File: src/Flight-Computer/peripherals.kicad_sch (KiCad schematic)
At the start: 34 parts, among them P10 Micro_SD_Card, P8 USB, P9 1984659, Q5 QS5U17TR, Q6 QS5U17TR, U10 TS391IYLT, U11 TS391IYLT, U6 SST25VF040B-50-4I-S2AE-T, U7 RFM95W-868S2, U8 CP2102-GMR(QFN28), U9 TS391IYLT

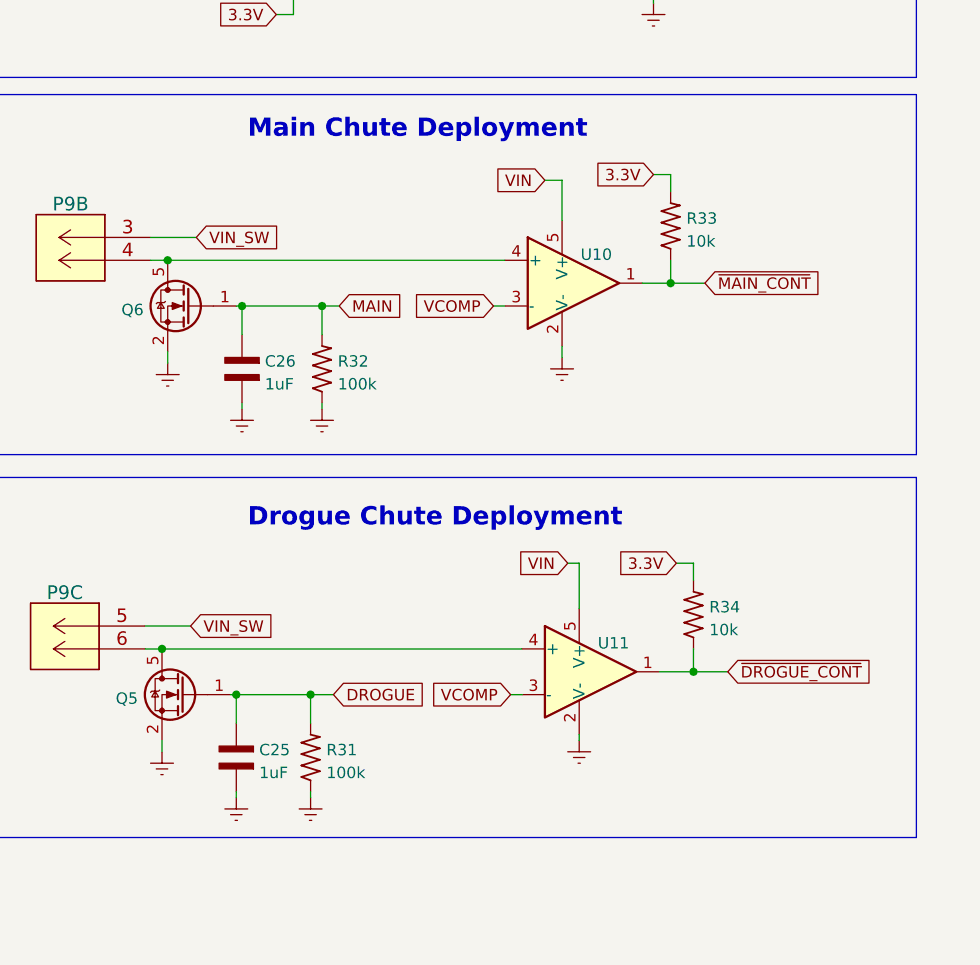
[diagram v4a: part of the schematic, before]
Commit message: added ignition continuity pull down resistors
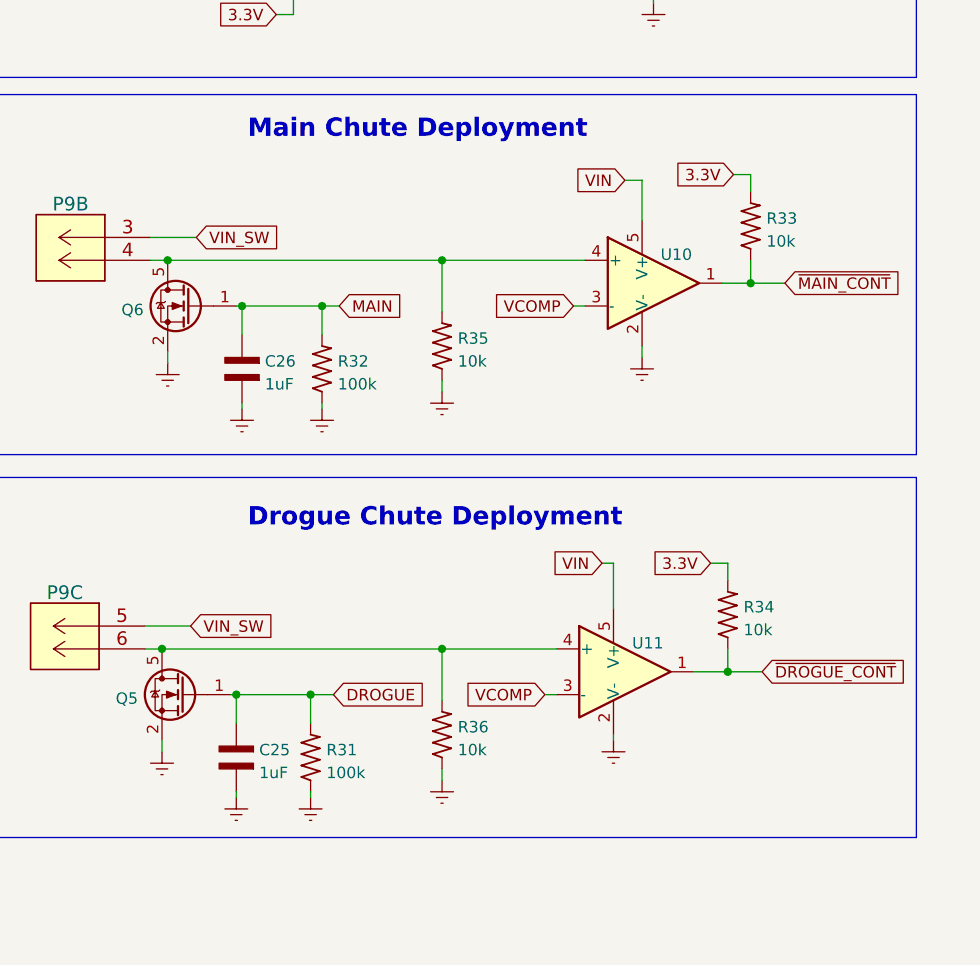
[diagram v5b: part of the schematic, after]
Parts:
- added R35, R36: 10k, Flight-Computer:RES_0603, symbol Flight-Computer:RES_0603
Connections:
- net Earth: now also R35.1, R36.1
- net at P9.6, Q5.5 (D), U11.4 (+): now also R36.2
- net at P9.4 (6), Q6.5 (D), U10.4 (+): now also R35.2
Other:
- moved on the sheet: R33, R34, U10, U11
